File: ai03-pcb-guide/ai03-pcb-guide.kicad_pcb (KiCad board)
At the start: 2 copper layers, 24 parts, among them SW1 SW_Push, U1 ATmega32U4-AU, Y1 16MHz

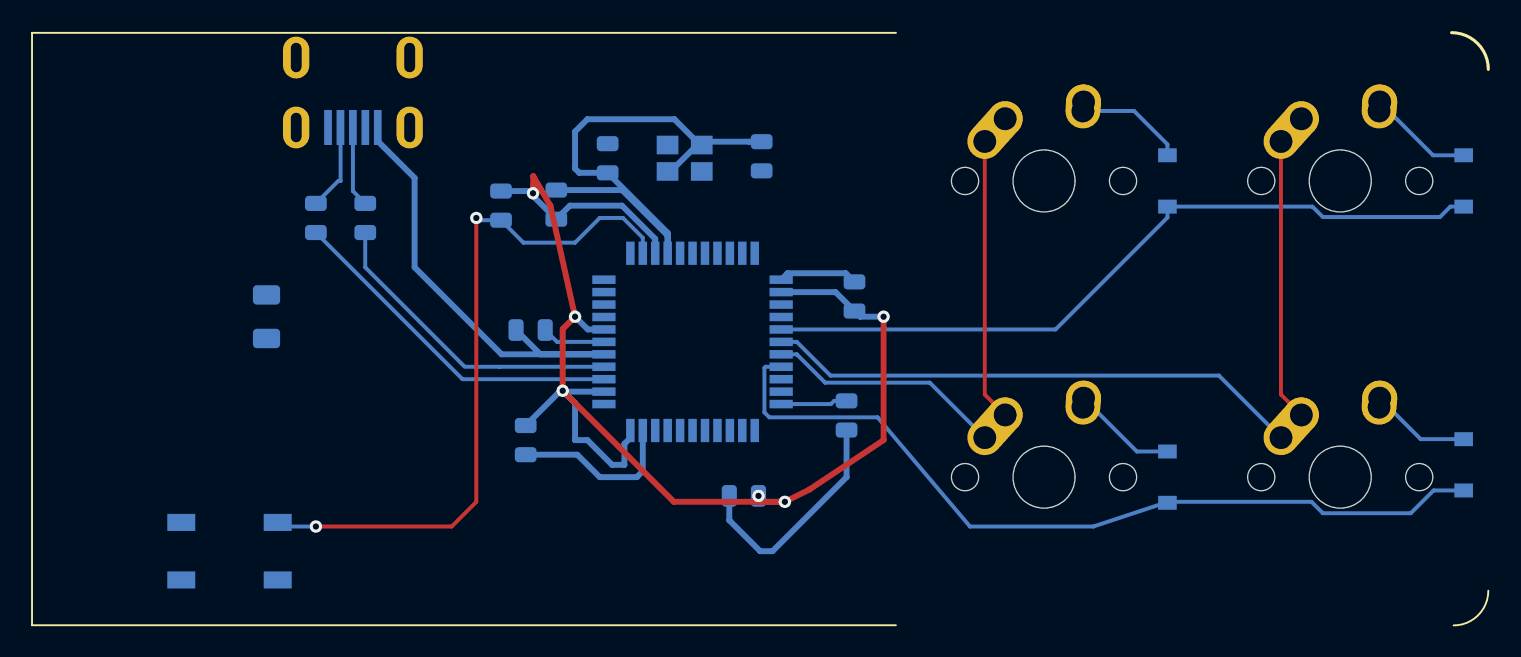
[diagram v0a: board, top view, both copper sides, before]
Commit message: ground fill
filled ground, made some new connections
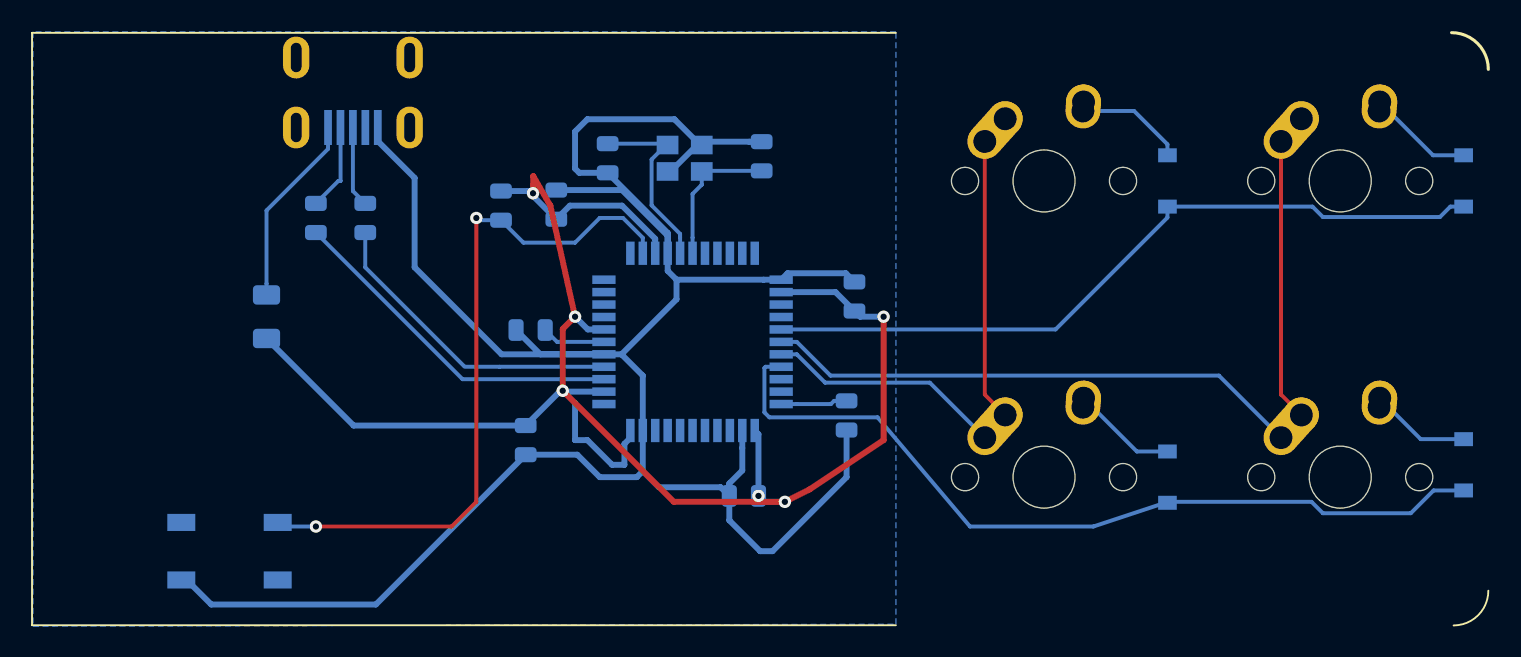
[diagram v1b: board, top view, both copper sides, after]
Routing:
- net GND: track 98.6 -> 157.7 mm
- net +5V: track 88.2 -> 111.5 mm
- net VCC: track 0.00 -> 12.4 mm
- net Net-(C2-Pad1): track 0.00 -> 12.1 mm
- net Net-(C1-Pad1): track 0.00 -> 9.38 mm
- added copper zone on B.Cu, net GND
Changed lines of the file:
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@@
     (thickness 1.6)
     (drawings 5)
-    (tracks 157)
+    (tracks 199)
     (zones 0)
     (modules 24)
@@
     (solder_mask_min_width 0.25)
     (aux_axis_origin 0 0)
-    (visible_elements FFFFFF7F)
+    (visible_elements 7FFFFFFF)
     (pcbplotparams
       (layerselection 0x010fc_ffffffff)
@@
   (segment (start 212.763 107.988) (end 219.344 107.988) (width 0.381) (layer B.Cu) (net 1))
   (segment (start 207.16875 102.39375) (end 212.763 107.988) (width 0.381) (layer B.Cu) (net 1))
+  (segment (start 192.5125 122.5) (end 194.0915 124.079) (width 0.381) (layer B.Cu) (net 1))
+  (segment (start 192.1625 122.5) (end 192.5125 122.5) (width 0.381) (layer B.Cu) (net 1))
+  (segment (start 204.67725 124.079) (end 214.3125 114.44375) (width 0.381) (layer B.Cu) (net 1))
+  (segment (start 194.0915 124.079) (end 204.67725 124.079) (width 0.381) (layer B.Cu) (net 1))
+  (segment (start 228.244 114.019) (end 228.244 112.888) (width 0.381) (layer B.Cu) (net 1))
+  (segment (start 228.244 115.4585) (end 228.244 114.019) (width 0.381) (layer B.Cu) (net 1))
+  (segment (start 227.4085 116.294) (end 228.244 115.4585) (width 0.381) (layer B.Cu) (net 1))
+  (segment (start 227.4085 117.094) (end 227.4085 116.294) (width 0.381) (layer B.Cu) (net 1))
+  (segment (start 222.882013 116.537763) (end 221.844 115.49975) (width 0.381) (layer B.Cu) (net 1))
+  (segment (start 226.852263 116.537763) (end 222.882013 116.537763) (width 0.381) (layer B.Cu) (net 1))
+  (segment (start 227.4085 117.094) (end 226.852263 116.537763) (width 0.381) (layer B.Cu) (net 1))
+  (segment (start 229.613 103.188) (end 230.744 103.188) (width 0.381) (layer B.Cu) (net 1))
+  (segment (start 224.013 103.188) (end 229.613 103.188) (width 0.381) (layer B.Cu) (net 1))
+  (segment (start 223.444 102.619) (end 224.013 103.188) (width 0.381) (layer B.Cu) (net 1))
+  (segment (start 223.444 101.488) (end 223.444 102.619) (width 0.381) (layer B.Cu) (net 1))
+  (segment (start 224.013 104.45) (end 224.013 103.188) (width 0.381) (layer B.Cu) (net 1))
+  (segment (start 220.475 107.988) (end 224.013 104.45) (width 0.381) (layer B.Cu) (net 1))
+  (segment (start 219.344 107.988) (end 220.475 107.988) (width 0.381) (layer B.Cu) (net 1))
+  (segment (start 221.844 109.357) (end 221.844 112.888) (width 0.381) (layer B.Cu) (net 1))
+  (segment (start 220.475 107.988) (end 221.844 109.357) (width 0.381) (layer B.Cu) (net 1))
+  (segment (start 225.044 100.484) (end 225.044 101.488) (width 0.254) (layer B.Cu) (net 2))
+  (segment (start 225.044 97.673) (end 225.044 100.484) (width 0.254) (layer B.Cu) (net 2))
+  (segment (start 225.636 97.081) (end 225.044 97.673) (width 0.254) (layer B.Cu) (net 2))
+  (segment (start 225.636 96.227) (end 225.636 97.081) (width 0.254) (layer B.Cu) (net 2))
+  (segment (start 225.6755 96.1875) (end 225.636 96.227) (width 0.254) (layer B.Cu) (net 2))
+  (segment (start 229.489 96.1875) (end 225.6755 96.1875) (width 0.254) (layer B.Cu) (net 2))
+  (segment (start 223.3485 94.4395) (end 223.436 94.527) (width 0.254) (layer B.Cu) (net 3))
+  (segment (start 219.583 94.4395) (end 223.3485 94.4395) (width 0.254) (layer B.Cu) (net 3))
+  (segment (start 224.244 100.484) (end 224.244 101.488) (width 0.254) (layer B.Cu) (net 3))
+  (segment (start 224.244 100.243632) (end 224.244 100.484) (width 0.254) (layer B.Cu) (net 3))
+  (segment (start 222.408999 98.408631) (end 224.244 100.243632) (width 0.254) (layer B.Cu) (net 3))
+  (segment (start 222.408999 95.454001) (end 222.408999 98.408631) (width 0.254) (layer B.Cu) (net 3))
+  (segment (start 223.336 94.527) (end 222.408999 95.454001) (width 0.254) (layer B.Cu) (net 3))
+  (segment (start 223.436 94.527) (end 223.336 94.527) (width 0.254) (layer B.Cu) (net 3))
   (segment (start 216.3295 107.188) (end 219.344 107.188) (width 0.254) (layer B.Cu) (net 4))
   (segment (start 215.5675 106.426) (end 216.3295 107.188) (width 0.254) (layer B.Cu) (net 4))
@@
   (segment (start 214.797475 96.528725) (end 215.9 98.425) (width 0.381) (layer F.Cu) (net 5))
   (segment (start 214.783243 97.63125) (end 214.797475 96.528725) (width 0.381) (layer F.Cu) (net 5))
+  (segment (start 203.24375 112.56875) (end 197.64375 106.96875) (width 0.381) (layer B.Cu) (net 5))
+  (segment (start 214.3125 112.56875) (end 203.24375 112.56875) (width 0.381) (layer B.Cu) (net 5))
+  (segment (start 229.2835 113.1275) (end 229.044 112.888) (width 0.381) (layer B.Cu) (net 5))
+  (segment (start 229.2835 117.094) (end 229.2835 113.1275) (width 0.381) (layer B.Cu) (net 5))
   (segment (start 253.4415 92.3375) (end 250.15 92.3375) (width 0.254) (layer B.Cu) (net 6))
   (segment (start 255.5875 94.4835) (end 253.4415 92.3375) (width 0.254) (layer B.Cu) (net 6))
@@
   (segment (start 271.87625 113.44375) (end 269.82 111.3875) (width 0.254) (layer B.Cu) (net 11))
   (segment (start 274.6375 113.44375) (end 271.87625 113.44375) (width 0.254) (layer B.Cu) (net 11))
+  (segment (start 197.64375 103.44375) (end 197.64375 104.16875) (width 0.254) (layer B.Cu) (net 12))
+  (segment (start 197.64375 98.73525) (end 197.64375 103.44375) (width 0.254) (layer B.Cu) (net 12))
+  (segment (start 201.6 94.779) (end 197.64375 98.73525) (width 0.254) (layer B.Cu) (net 12))
+  (segment (start 201.6 93.4) (end 201.6 94.779) (width 0.254) (layer B.Cu) (net 12))
   (segment (start 243.84 110.5775) (end 245.15 111.8875) (width 0.254) (layer F.Cu) (net 13))
   (segment (start 243.84 94.2975) (end 243.84 110.5775) (width 0.254) (layer F.Cu) (net 13))
@@
   (segment (start 234.15 110.98125) (end 233.94325 111.188) (width 0.254) (layer B.Cu) (net 20))
   (segment (start 234.95 110.98125) (end 234.15 110.98125) (width 0.254) (layer B.Cu) (net 20))
+  (zone (net 1) (net_name GND) (layer B.Cu) (hatch edge 0.508)
+    (connect_pads (clearance 0.508))
+    (min_thickness 0.254)
+    (fill yes (arc_segments 32) (thermal_gap 0.508) (thermal_bridge_width 0.508))
+    (polygon
+      (pts
+        (xy 238.125 87.249) (xy 182.626 87.249) (xy 182.626 125.476) (xy 238.125 125.349)
+      )
+    )
+  )
 )
